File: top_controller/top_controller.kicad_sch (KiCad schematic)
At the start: 112 parts, among them J1 OUT1, J10 USB_C_Receptacle_USB2.0, J11 SWD, J12 UART, J13 BOOT0, J2 OUT2, J3 OUT3, J4 OUT4, J5 OUT5, J6 OUT6, J7 OUT7, J8 OUT8, J9 PIN, SW1 RESET, U1 STM32F103C8Tx, U2 LT3045xMSE, U3 AD5754BREZ, U4 AD5754BREZ, U5 REF192, U6 EPM78V2, Y1 8MHz

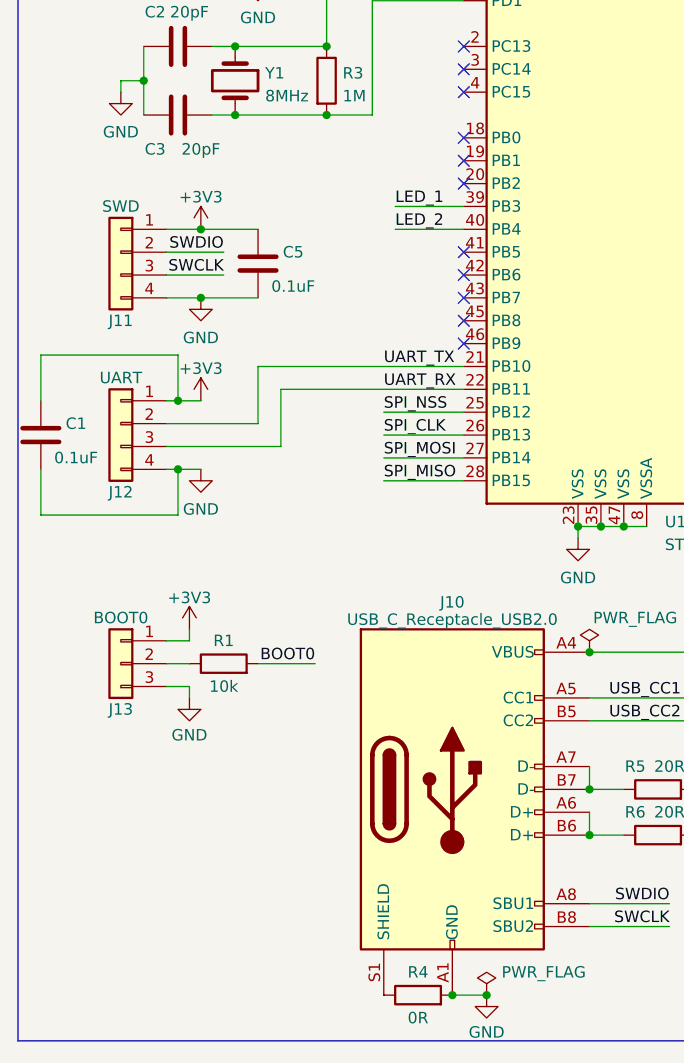
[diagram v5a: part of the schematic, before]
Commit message: Added BOOT1
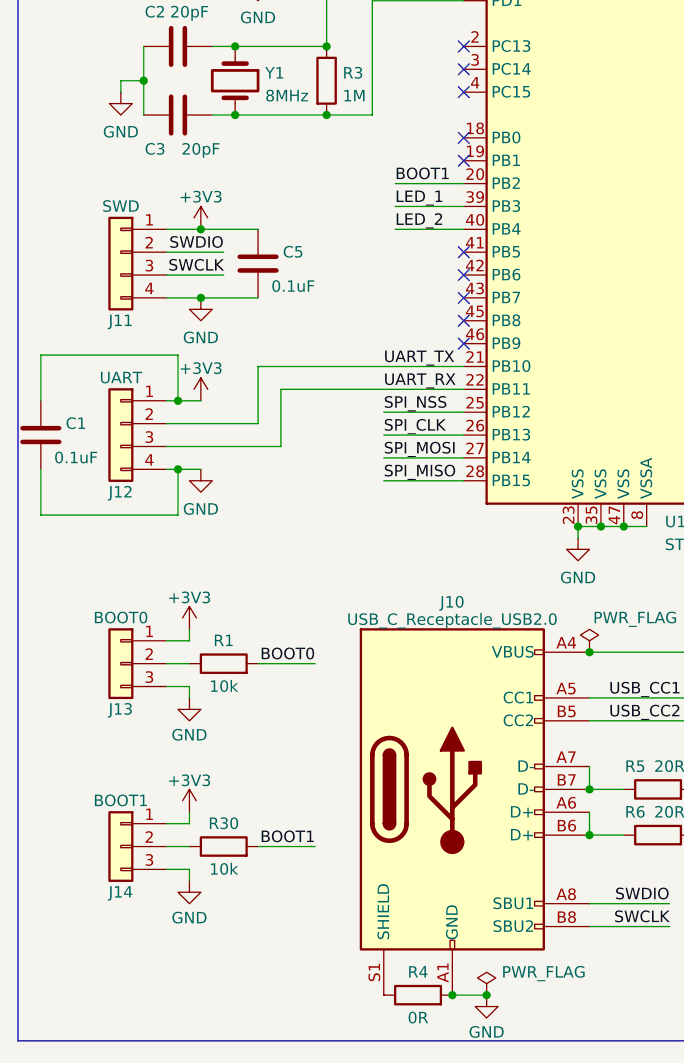
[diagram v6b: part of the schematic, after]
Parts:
- added J14: BOOT1, Connector_PinHeader_2.54mm:PinHeader_1x03_P2.54mm_Vertical, symbol Connector_Generic:Conn_01x03
- added R30: 10k, Resistor_SMD:R_0603_1608Metric, symbol Device:R
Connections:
- net +3V3: now also J14.1 (Pin_1)
- net GND: now also J14.3 (Pin_3)
- net BOOT1: now reaches U1.20 (PB2)
- net BOOT1: now also R30.2
- new net: J14.2 (Pin_2), R30.1
- no-connect marks 21 -> 20
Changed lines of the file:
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@@
   (no_connect (at 63.5 77.47))
   (no_connect (at 265.43 48.26))
-  (no_connect (at 63.5 69.85))
   (no_connect (at 63.5 80.01))
   (no_connect (at 199.39 45.72))
@@
     (stroke (width 0) (type default))
   )
+  (wire (pts (xy 40.64 143.51) (xy 46.99 143.51))
+    (stroke (width 0) (type default))
+  )
   (wire (pts (xy 130.81 66.04) (xy 133.35 66.04))
     (stroke (width 0) (type default))
@@
     (stroke (width 0) (type default))
   )
+  (wire (pts (xy 33.02 140.97) (xy 33.02 139.7))
+    (stroke (width 0) (type default))
+  )
   (wire (pts (xy 165.1 156.21) (xy 165.1 152.4))
     (stroke (width 0) (type default))
@@
     (stroke (width 0) (type default))
   )
+  (wire (pts (xy 33.02 147.32) (xy 33.02 146.05))
+    (stroke (width 0) (type default))
+  )
   (wire (pts (xy 144.78 53.34) (xy 153.67 53.34))
     (stroke (width 0) (type default))
@@
     (stroke (width 0) (type default))
   )
+  (wire (pts (xy 30.48 143.51) (xy 33.02 143.51))
+    (stroke (width 0) (type default))
+  )
   (wire (pts (xy 207.01 83.82) (xy 199.39 83.82))
     (stroke (width 0) (type default))
@@
     (stroke (width 0) (type default))
   )
+  (wire (pts (xy 33.02 146.05) (xy 30.48 146.05))
+    (stroke (width 0) (type default))
+  )
   (wire (pts (xy 54.61 95.25) (xy 63.5 95.25))
     (stroke (width 0) (type default))
@@
     (stroke (width 0) (type default))
   )
+  (wire (pts (xy 30.48 140.97) (xy 33.02 140.97))
+    (stroke (width 0) (type default))
+  )
   (wire (pts (xy 196.85 105.41) (xy 196.85 101.6))
     (stroke (width 0) (type default))
@@
   )
   (wire (pts (xy 86.36 29.21) (xy 97.79 29.21))
+    (stroke (width 0) (type default))
+  )
+  (wire (pts (xy 55.88 69.85) (xy 63.5 69.85))
     (stroke (width 0) (type default))
   )
@@
     (effects (font (size 1.27 1.27)) (justify right bottom))
   )
+  (label "BOOT1" (at 55.88 69.85 0) (fields_autoplaced)
+    (effects (font (size 1.27 1.27)) (justify left bottom))
+  )
   (label "AVSS" (at 278.13 73.66 180) (fields_autoplaced)
     (effects (font (size 1.27 1.27)) (justify right bottom))
@@
   (label "NRST" (at 54.61 36.83 0) (fields_autoplaced)
     (effects (font (size 1.27 1.27)) (justify left bottom))
+  )
+  (label "BOOT1" (at 46.99 143.51 180) (fields_autoplaced)
+    (effects (font (size 1.27 1.27)) (justify right bottom))
   )
   (symbol (lib_id "Device:C") (at 214.63 62.23 0) (unit 1)
@@
         (path "/7c6b3c3f-4f4f-428a-ae03-0b6a4ac321c8"
           (reference "#PWR015") (unit 1)
+        )
+      )
+    )
+  )
+  (symbol (lib_id "power:+3V3") (at 33.02 139.7 0) (unit 1)
+    (in_bom yes) (on_board yes) (dnp no) (fields_autoplaced)
+    (property "Reference" "#PWR030" (at 33.02 143.51 0)
+      (effects (font (size 1.27 1.27)) hide)
+    )
+    (property "Value" "+3V3" (at 33.02 136.1981 0)
+      (effects (font (size 1.27 1.27)))
+    )
+    (property "Footprint" "" (at 33.02 139.7 0)
+      (effects (font (size 1.27 1.27)) hide)
+    )
+    (property "Datasheet" "" (at 33.02 139.7 0)
+      (effects (font (size 1.27 1.27)) hide)
+    )
+    (pin "1")
+    (instances
+      (project "top_controller"
+        (path "/7c6b3c3f-4f4f-428a-ae03-0b6a4ac321c8"
+          (reference "#PWR030") (unit 1)
         )
       )
@@
     )
   )
+  (symbol (lib_id "Device:R") (at 36.83 143.51 90) (unit 1)
+    (in_bom yes) (on_board yes) (dnp no)
+    (property "Reference" "R30" (at 36.83 140.97 90)
+      (effects (font (size 1.27 1.27)))
+    )
+    (property "Value" "10k" (at 36.83 146.05 90)
+      (effects (font (size 1.27 1.27)))
+    )
+    (property "Footprint" "Resistor_SMD:R_0603_1608Metric" (at 36.83 145.288 90)
+      (effects (font (size 1.27 1.27)) hide)
+    )
+    (property "Datasheet" "~" (at 36.83 143.51 0)
+      (effects (font (size 1.27 1.27)) hide)
+    )
+    (pin "1")
+    (pin "2")
+    (instances
+      (project "top_controller"
+        (path "/7c6b3c3f-4f4f-428a-ae03-0b6a4ac321c8"
+          (reference "R30") (unit 1)
+        )
+      )
+    )
+  )
   (symbol (lib_id "Device:R") (at 97.79 146.05 0) (unit 1)
     (in_bom yes) (on_board yes) (dnp no) (fields_autoplaced)
@@
     )
   )
+  (symbol (lib_id "Connector_Generic:Conn_01x03") (at 25.4 143.51 0) (mirror y) (unit 1)
+    (in_bom yes) (on_board yes) (dnp no)
+    (property "Reference" "J14" (at 25.4 148.59 0)
+      (effects (font (size 1.27 1.27)))
+    )
+    (property "Value" "BOOT1" (at 25.4 138.43 0)
+      (effects (font (size 1.27 1.27)))
+    )
+    (property "Footprint" "Connector_PinHeader_2.54mm:PinHeader_1x03_P2.54mm_Vertical" (at 25.4 143.51 0)
+      (effects (font (size 1.27 1.27)) hide)
+    )
+    (property "Datasheet" "~" (at 25.4 143.51 0)
+      (effects (font (size 1.27 1.27)) hide)
+    )
+    (pin "1")
+    (pin "2")
+    (pin "3")
+    (instances
+      (project "top_controller"
+        (path "/7c6b3c3f-4f4f-428a-ae03-0b6a4ac321c8"
+          (reference "J14") (unit 1)
+        )
+      )
+    )
+  )
   (symbol (lib_id "Connector:Conn_Coaxial") (at 222.25 100.33 0) (mirror y) (unit 1)
     (in_bom yes) (on_board yes) (dnp no)
@@
         )
       )
+    )
+  )
+  (symbol (lib_id "power:GND") (at 33.02 147.32 0) (unit 1)
+    (in_bom yes) (on_board yes) (dnp no) (fields_autoplaced)
+    (property "Reference" "#PWR031" (at 33.02 153.67 0)
+      (effects (font (size 1.27 1.27)) hide)
+    )
+    (property "Value" "GND" (at 33.02 151.4555 0)
+      (effects (font (size 1.27 1.27)))
+    )
+    (property "Footprint" "" (at 33.02 147.32 0)
+      (effects (font (size 1.27 1.27)) hide)
+    )
+    (property "Datasheet" "" (at 33.02 147.32 0)
+      (effects (font (size 1.27 1.27)) hide)
+    )
+    (pin "1")
+    (instances
+      (project "top_controller"
+        (path "/7c6b3c3f-4f4f-428a-ae03-0b6a4ac321c8"
+          (reference "#PWR031") (unit 1)
+        )
+      )

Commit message: Part of the board is done
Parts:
- D1: value CH1 -> LED1
- D2: value CH2 -> LED2
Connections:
- net +3V3: now also D11.2 (A); no longer R11.2, R12.2, R13.2, R14.2, R15.2, R16.2, R17.2, R18.2, R19.2, R20.2, R21.2
- net AVDD: now also U6.3 (Vout); no longer U6. (Vout)
- net AVSS: now also U6.2 (GND); no longer U6. (Vout)
- net GND: now also R11.2, R12.2, R13.2, R14.2, R15.2, R16.2, R17.2, R18.2, R19.2, R20.2, R21.1, R22.1; no longer D11.1 (K), D12.1 (K)
- net LED_1: now also D1.2 (A); no longer D1.1 (K)
- net LED_2: now also D2.2 (A); no longer D2.1 (K)
- net LED_CH1: now also D3.2 (A); no longer D3.1 (K)
- net LED_CH2: now also D4.2 (A); no longer D4.1 (K)
- net LED_CH3: now also D5.2 (A); no longer D5.1 (K)
- net LED_CH4: now also D6.2 (A); no longer D6.1 (K)
- net LED_CH5: now also D7.2 (A); no longer D7.1 (K)
- net LED_CH6: now also D8.2 (A); no longer D8.1 (K)
- net LED_CH7: now also D9.2 (A); no longer D9.1 (K)
- net LED_CH8: now also D10.2 (A); no longer D10.1 (K)
- net UART_RX: now also U1.43 (PB7); no longer U1.22 (PB11)
- net UART_TX: now also U1.42 (PB6); no longer U1.21 (PB10)
- net USB_VBUS: now also D12.2 (A); no longer R22.2
- net at R16.1: now also D6.1 (K); no longer D6.2 (A)
- net at R17.1: now also D7.1 (K); no longer D7.2 (A)
- net at R12.1: now also D2.1 (K); no longer D2.2 (A)
- net at R15.1: now also D5.1 (K); no longer D5.2 (A)
- net at R11.1: now also D1.1 (K); no longer D1.2 (A)
- net at R19.1: now also D9.1 (K); no longer D9.2 (A)
- net at R18.1: now also D8.1 (K); no longer D8.2 (A)
- net at R14.1: now also D4.1 (K); no longer D4.2 (A)
- net at R13.1: now also D3.1 (K); no longer D3.2 (A)
- net at R20.1: now also D10.1 (K); no longer D10.2 (A)
- new net: D11.1 (K), R21.2
- new net: D12.1 (K), R22.2
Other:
- moved on the sheet: D1, D10, D11, D12, D2, D3, D4, D5, D6, D7, D8, D9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

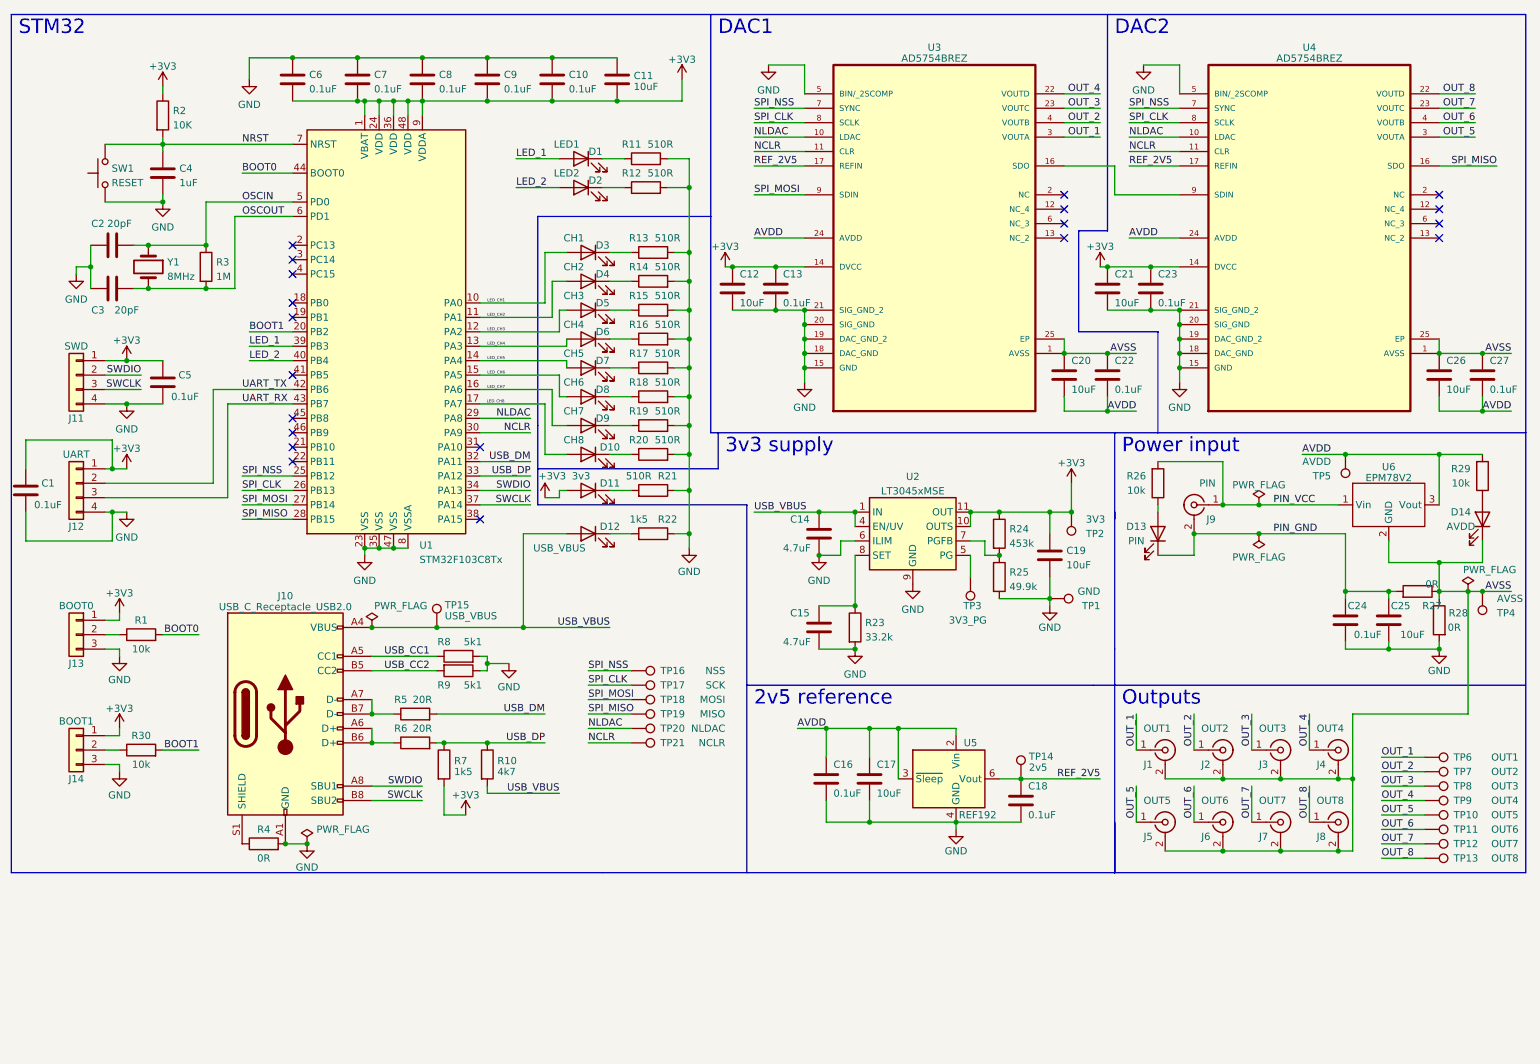
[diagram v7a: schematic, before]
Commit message: Added second voltage reference
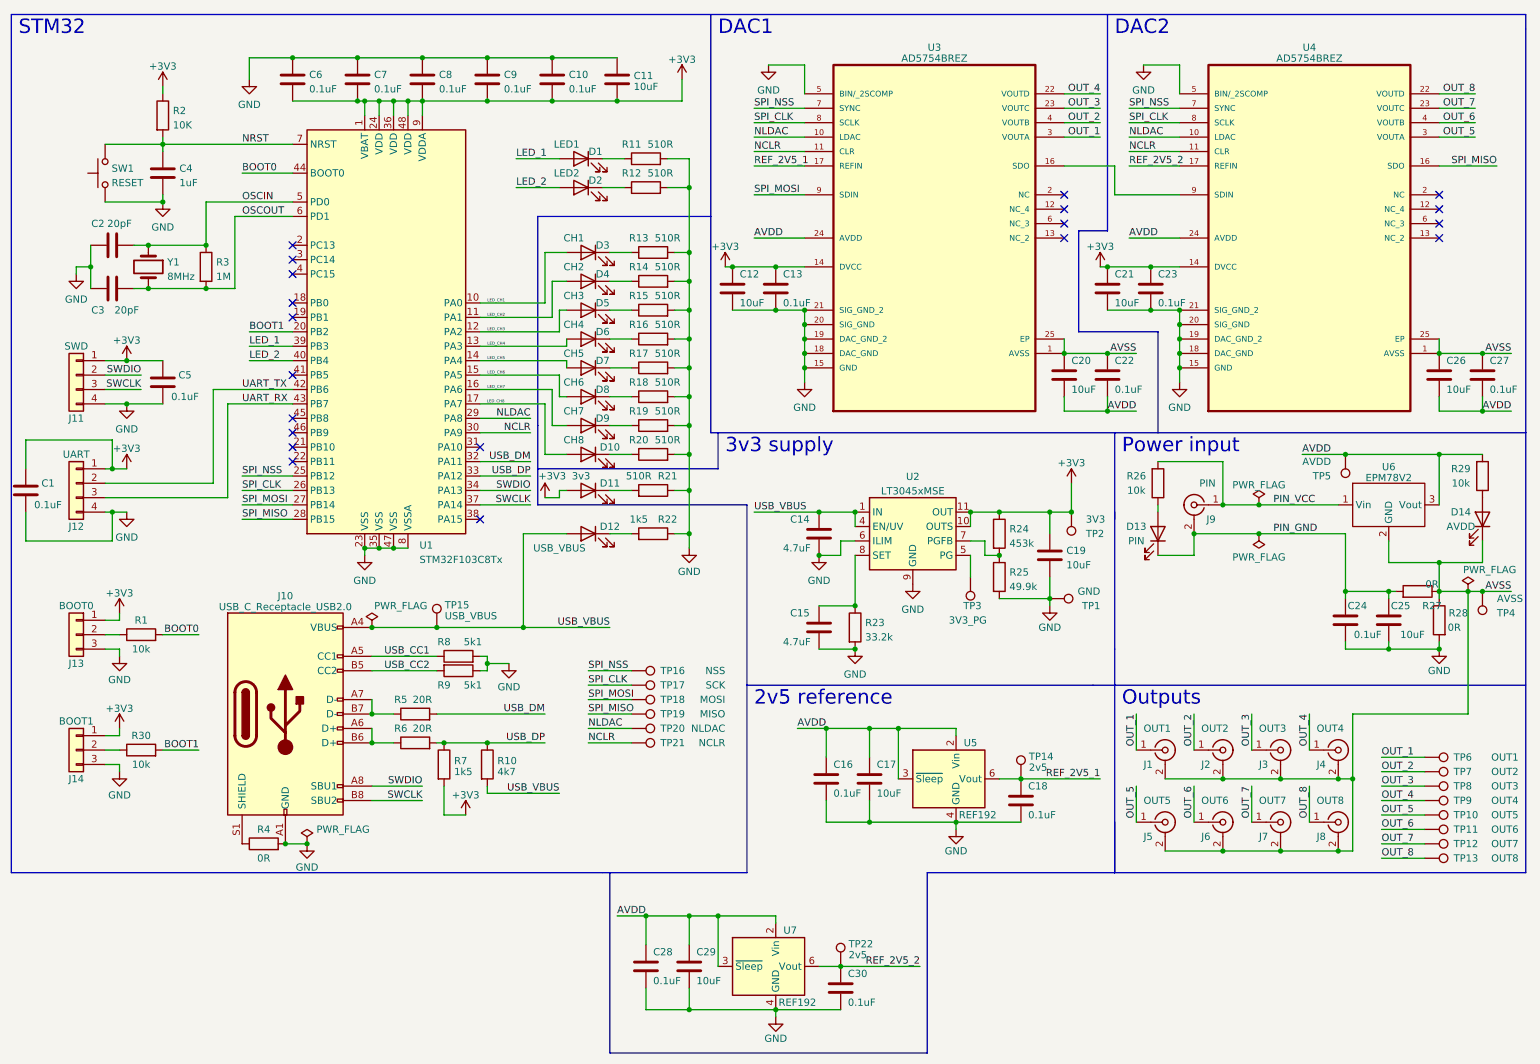
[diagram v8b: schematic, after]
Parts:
- added C28, C30: 0.1uF, Capacitor_SMD:C_0603_1608Metric, symbol Device:C
- added C29: 10uF, Capacitor_SMD:C_1206_3216Metric, symbol Device:C
- added TP22: 2v5, TestPoint:TestPoint_Keystone_5010-5014_Multipurpose, symbol Connector:TestPoint
- added U7: REF192, Package_SO:SOIC-8_3.9x4.9mm_P1.27mm, symbol Reference_Voltage:REF192
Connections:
- net AVDD: now also C28.1, C29.1, U7.2 (Vin), U7.3 (~{Sleep})
- net GND: now also C28.2, C29.2, C30.2, U7.4 (GND)
- net REF_2V5 renamed REF_2V5_1
- net REF_2V5_1: no longer U4.17 (REFIN)
- new net REF_2V5_2: C30.1, TP22.1, U4.17 (REFIN), U7.6 (Vout)
